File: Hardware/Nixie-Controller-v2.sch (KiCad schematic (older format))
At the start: 218 parts, among them J7 12V DC JACK, U1 MAX1771, U10 74HC4067, U11 M41T01, U12 STM32F103C8, U13 OPA180, U14 74HC4067, U15 OPA180, U16 74HC4067, U17 OPA180, U18 74HC4067, U19 OPA180, U2 BH2226, U20 74HC4067, U21 OPA180, U22 74HC4067, U3 74HC595, U4 74HC595, U5 74HC595, U6 SN74LVCC3245A, U7 NCP1117-5.0, U8 NCP1117-3.3, U9 OPA180, Y1 32.768KHz

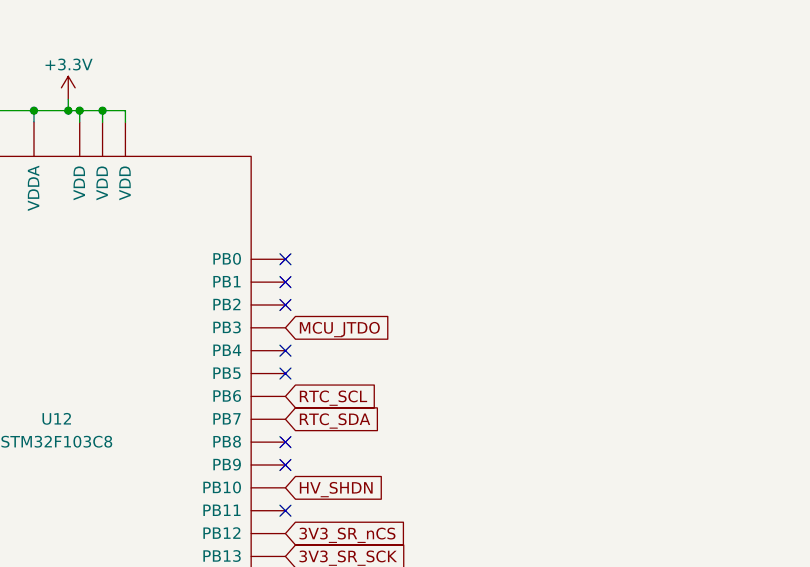
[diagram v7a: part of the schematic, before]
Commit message: Add reset jumper
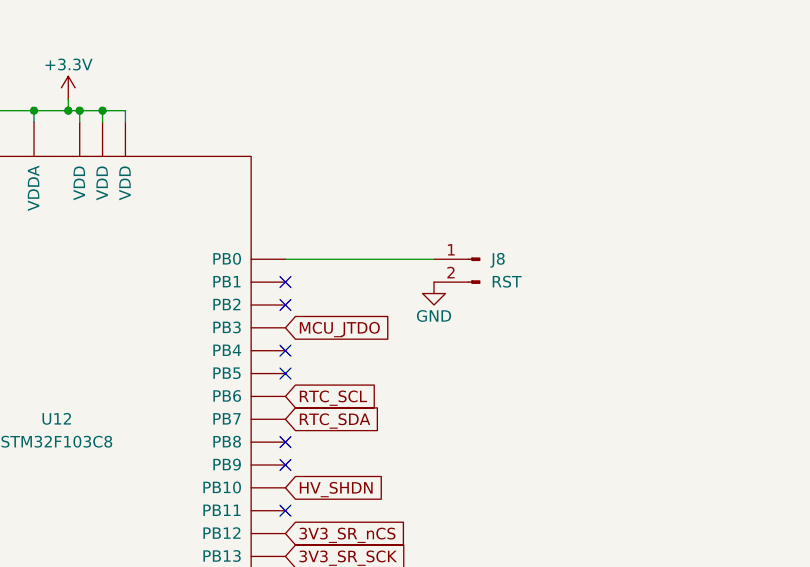
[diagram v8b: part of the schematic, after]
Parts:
- added J8: RST, Connector_PinHeader_2.54mm:PinHeader_1x02_P2.54mm_Vertical, symbol Connector:Conn_01x02_Male
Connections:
- net GND: now also J8.2 (Pin_2)
- net at U12.18 (PB0): now also J8.1 (Pin_1)
- no-connect marks 78 -> 77
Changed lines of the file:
@@
 	1    0    0    -1
 $EndComp
-NoConn ~ 18050 8100
 NoConn ~ 18050 8200
 NoConn ~ 18050 8300
@@
 WIFI
 NoConn ~ 18050 9200
+$Comp
+L Connector:Conn_01x02_Male J8
+U 1 1 6194C683
+P 18900 8100
+F 0 "J8" H 18850 8100 50  0000 R CNN
+F 1 "RST" H 18850 8000 50  0000 R CNN
+F 2 "Connector_PinHeader_2.54mm:PinHeader_1x02_P2.54mm_Vertical" H 18900 8100 50  0001 C CNN
+F 3 "~" H 18900 8100 50  0001 C CNN
+	1    18900 8100
+	-1   0    0    -1
+$EndComp
+Wire Wire Line
+	18050 8100 18700 8100
+$Comp
+L power:GND #PWR0124
+U 1 1 61A14F98
+P 18700 8200
+F 0 "#PWR0124" H 18700 7950 50  0001 C CNN
+F 1 "GND" H 18700 8050 50  0000 C CNN
+F 2 "" H 18700 8200 50  0001 C CNN
+F 3 "" H 18700 8200 50  0001 C CNN
+	1    18700 8200
+	1    0    0    -1
+$EndComp
 $EndSCHEMATC
